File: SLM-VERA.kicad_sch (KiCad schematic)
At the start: 25 parts, among them J1 FH35C-45S-0.3SHW(50), J2 FH35C-45S-0.3SHW(50), U1 FODM217D, U2 FODM217D, U3 FODM217D, U4 ESP32-DevKitC

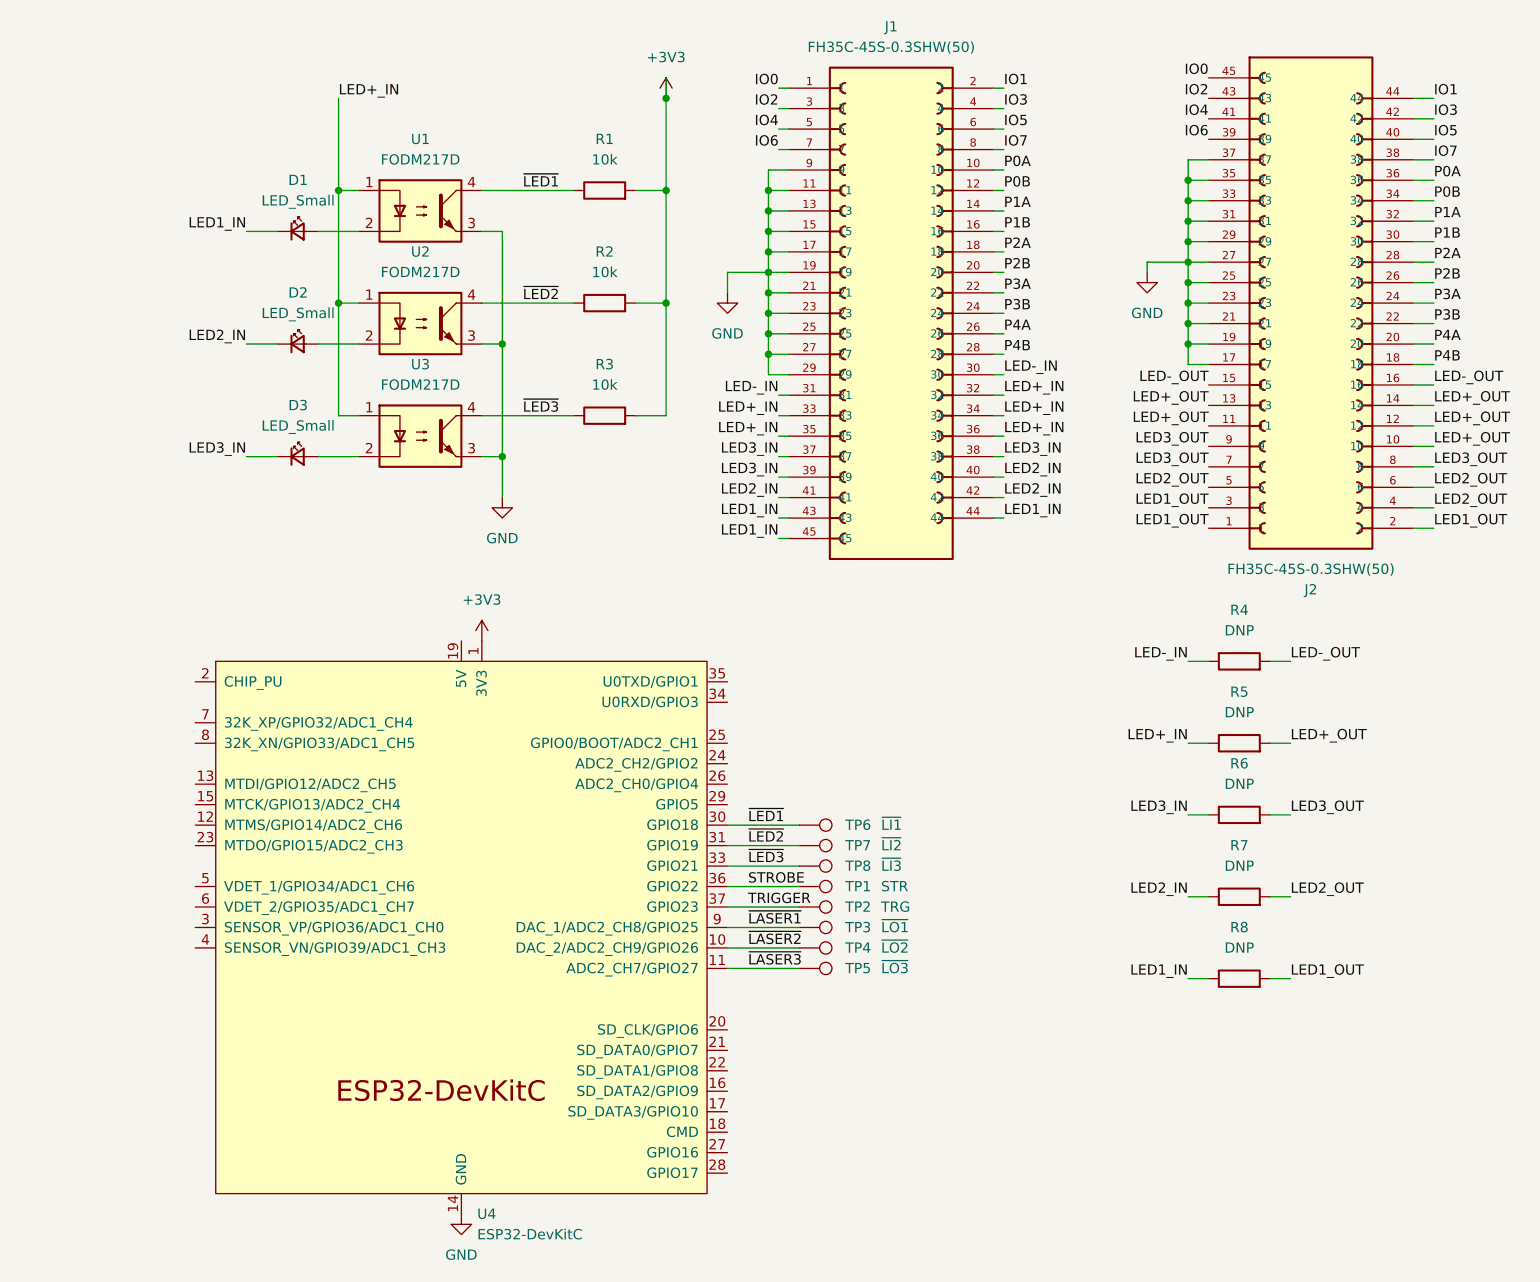
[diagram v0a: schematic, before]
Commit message: changed ESP32-Devkit-C to Seeeduino Xiao
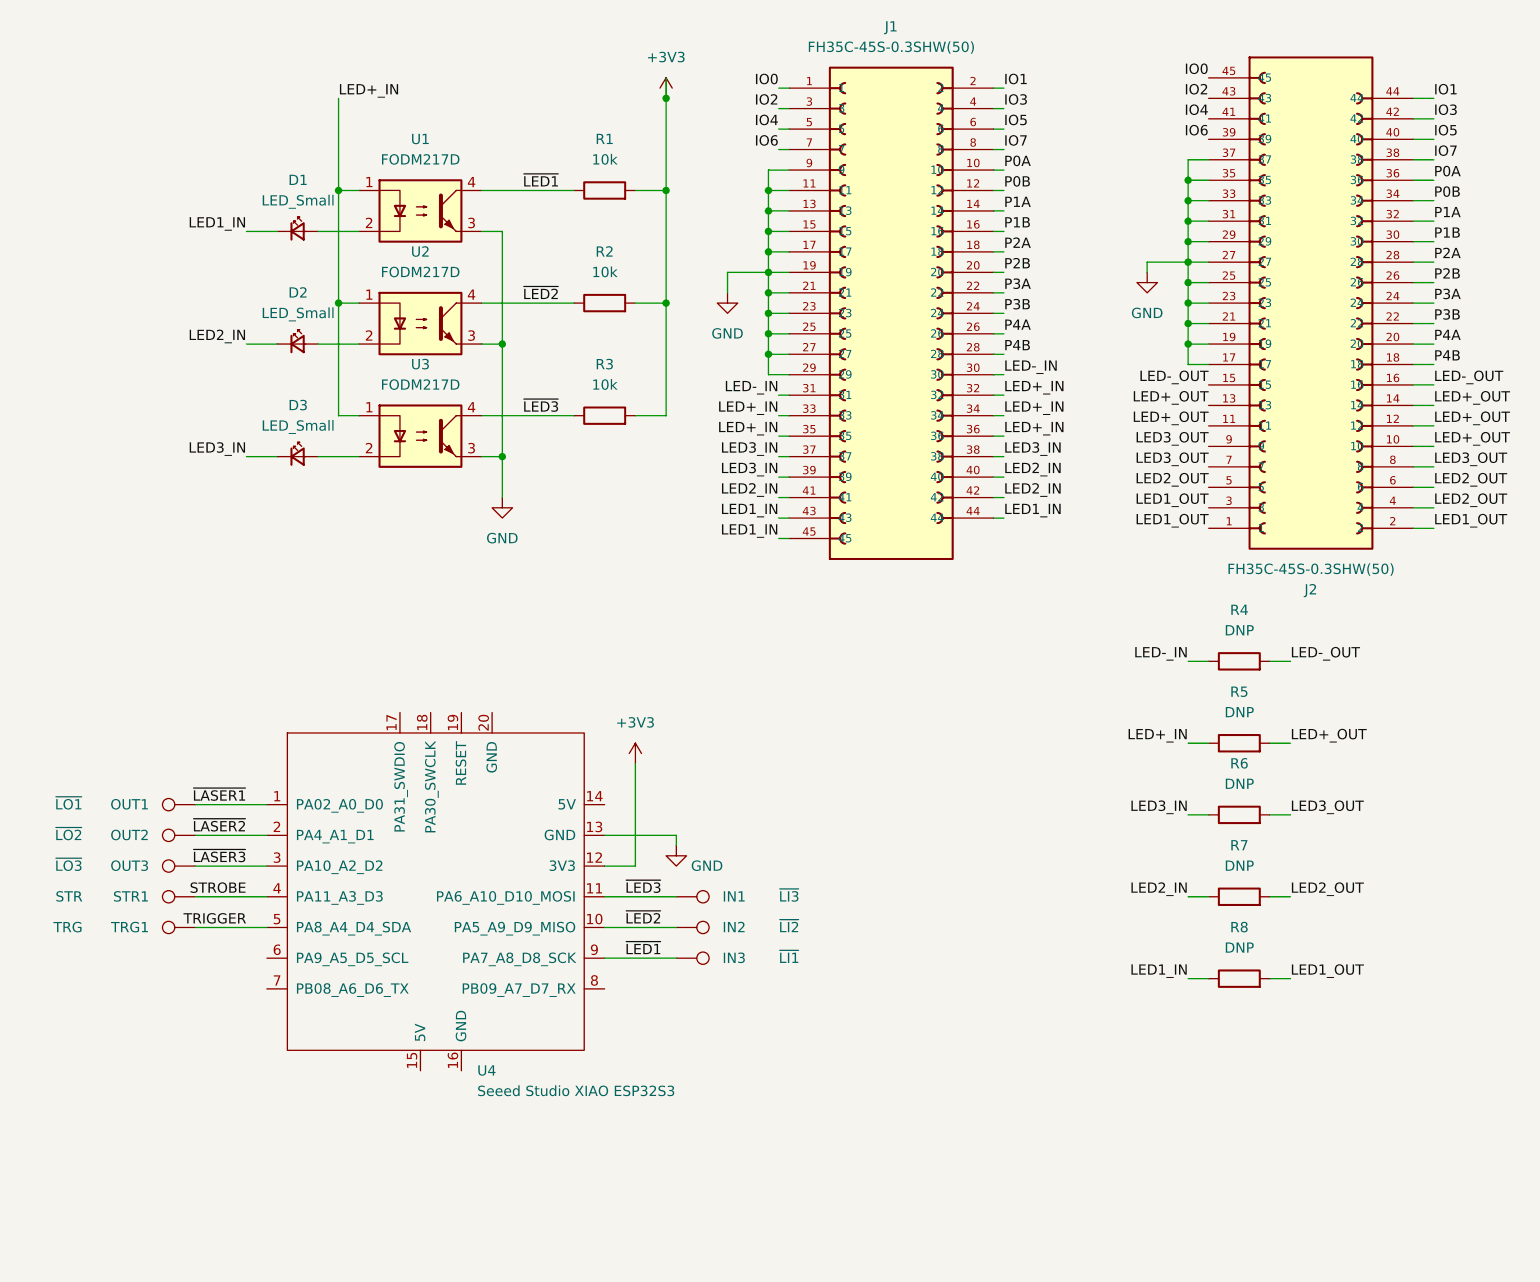
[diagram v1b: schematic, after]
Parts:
- removed U4: ESP32-DevKitC, PCM_Espressif:ESP32-DevKitC, symbol Espressif:ESP32-DevKitC
- added U4: Seeed Studio XIAO ESP32S3, Seeed Studio XIAO Series Library:XIAO-Generic-Hybrid-14P-2.54-21X17.8MM, symbol Seeed_Studio_XIAO_Series:Seeed Studio XIAO SAMD21
- renumbered TP8 to IN1, TP7 to IN2, TP6 to IN3, TP3 to OUT1, TP4 to OUT2, TP5 to OUT3, TP1 to STR1, TP2 to TRG1
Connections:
- net +3V3: now also U4.12 (3V3)
- net GND: now also U4.13 (GND)
- net STROBE: now also U4.4 (PA11_A3_D3)
- net TRIGGER: now also U4.5 (PA8_A4_D4_SDA)
- net ~{LASER1}: now also U4.1 (PA02_A0_D0)
- net ~{LASER2}: now also U4.2 (PA4_A1_D1)
- net ~{LASER3}: now also U4.3 (PA10_A2_D2)
- net ~{LED1}: now also U4.9 (PA7_A8_D8_SCK)
- net ~{LED2}: now also U4.10 (PA5_A9_D9_MISO)
- net ~{LED3}: now also U4.11 (PA6_A10_D10_MOSI)
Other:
- moved on the sheet: IN1, IN2, IN3, OUT1, OUT2, OUT3, STR1, TRG1
